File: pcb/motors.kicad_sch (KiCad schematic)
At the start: 21 parts, among them J4 Conn_01x02_Pin, J5 Conn_01x02_Pin, J6 Conn_01x02_Pin, J7 Conn_01x02_Pin, J8 Conn_01x02_Pin, Q1 AO3400A, U3 DRV8833PWP, U4 DRV8833PWP

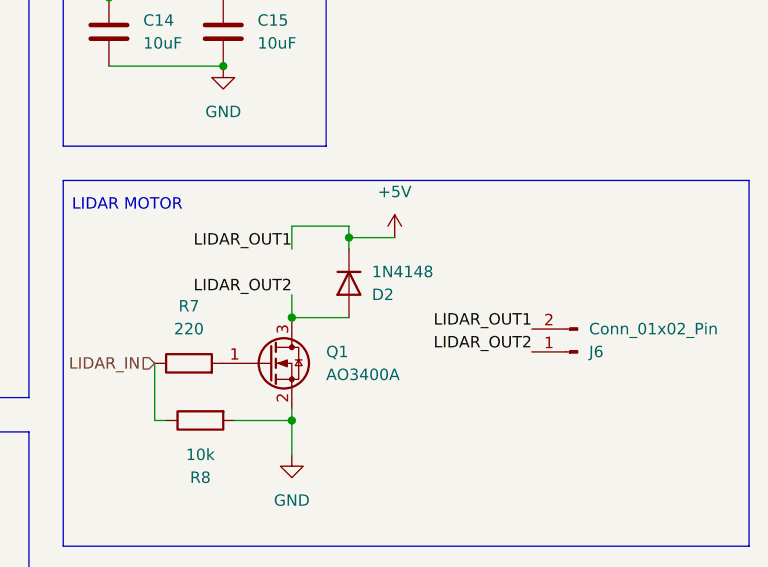
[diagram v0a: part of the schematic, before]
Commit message: update diode, usb routing
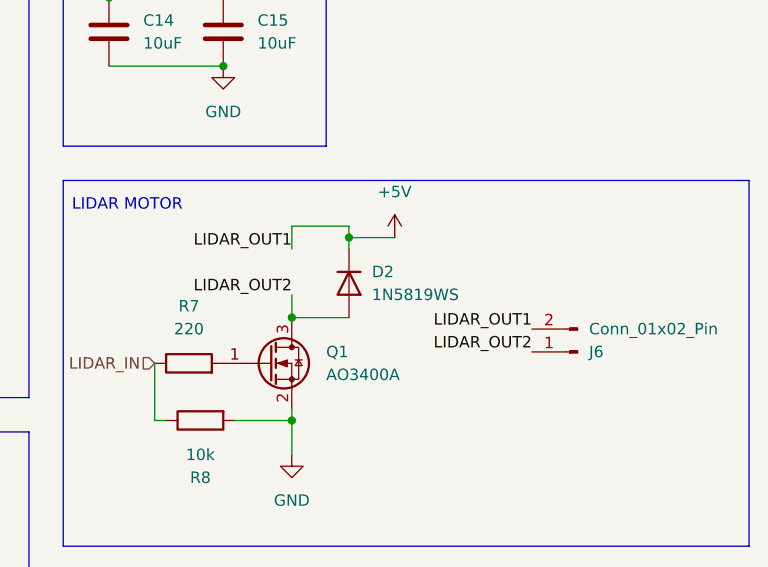
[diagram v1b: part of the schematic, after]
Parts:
- D2: value 1N4148 -> 1N5819WS; footprint Diode_SMD:D_SOD-323_HandSoldering -> Diode_SMD:D_SOD-123; LCSC C41371421 -> C8598
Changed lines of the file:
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@@
+	)
+	(symbol
+		(lib_id "Device:D")
+		(at 142.24 63.5 270)
+		(unit 1)
+		(body_style 1)
+		(exclude_from_sim no)
+		(in_bom no)
+		(on_board yes)
+		(in_pos_files yes)
+		(dnp no)
+		(fields_autoplaced yes)
+		(property "Reference" "D2"
+			(at 144.78 62.2299 90)
+			(show_name no)
+			(do_not_autoplace no)
+			(effects
+				(font
+					(size 1.27 1.27)
+				)
+				(justify left)
+			)
+		)
+		(property "Value" "1N5819WS"
+			(at 144.78 64.7699 90)
+			(show_name no)
+			(do_not_autoplace no)
+			(effects
+				(font
+					(size 1.27 1.27)
+				)
+				(justify left)
+			)
+		)
+		(property "Footprint" "Diode_SMD:D_SOD-123"
+			(at 142.24 63.5 0)
+			(hide yes)
+			(show_name no)
+			(do_not_autoplace no)
+			(effects
+				(font
+					(size 1.27 1.27)
+				)
+			)
+		)
+		(property "Datasheet" ""
+			(at 142.24 63.5 0)
+			(hide yes)
+			(show_name no)
+			(do_not_autoplace no)
+			(effects
+				(font
+					(size 1.27 1.27)
+				)
+			)
+		)
+		(property "Description" "Diode"
+			(at 142.24 63.5 0)
+			(hide yes)
+			(show_name no)
+			(do_not_autoplace no)
+			(effects
+				(font
+					(size 1.27 1.27)
+				)
+			)
+		)
+		(property "Sim.Device" "D"
+			(at 142.24 63.5 0)
+			(hide yes)
+			(show_name no)
+			(do_not_autoplace no)
+			(effects
+				(font
+					(size 1.27 1.27)
+				)
+			)
+		)
+		(property "Sim.Pins" "1=K 2=A"
+			(at 142.24 63.5 0)
+			(hide yes)
+			(show_name no)
+			(do_not_autoplace no)
+			(effects
+				(font
+					(size 1.27 1.27)
+				)
+			)
+		)
+		(property "LCSC" "C8598"
+			(at 142.24 63.5 0)
+			(hide yes)
+			(show_name no)
+			(do_not_autoplace no)
+			(effects
+				(font
+					(size 1.27 1.27)
+				)
+			)
+		)
+		(property "KLC_S3.3" ""
+			(at 142.24 63.5 0)
+			(hide yes)
+			(show_name no)
+			(do_not_autoplace no)
+			(effects
+				(font
+					(size 1.27 1.27)
+				)
+			)
+		)
+		(property "KLC_S4.1" ""
+			(at 142.24 63.5 0)
+			(hide yes)
+			(show_name no)
+			(do_not_autoplace no)
+			(effects
+				(font
+					(size 1.27 1.27)
+				)
+			)
+		)
+		(pin "2"
+		)
+		(pin "1"
+		)
+		(instances
+			(project "slam"
+				(path "/d9b72bf7-a9fc-47a9-9340-f48fc87a9331/33a751a0-247f-4347-86aa-bb0fbce908f1"
+					(reference "D2")
+					(unit 1)
+				)
+			)
+		)
 	)
 	(symbol
@@
 					(unit 1)
 				)
-			)
-		)
-	)
-	(symbol
-		(lib_id "Device:D")
-		(at 142.24 63.5 90)
-		(mirror x)
-		(unit 1)
-		(body_style 1)
-		(exclude_from_sim no)
-		(in_bom no)
-		(on_board yes)
-		(in_pos_files yes)
-		(dnp no)
-		(property "Reference" "D2"
-			(at 144.78 64.7701 90)
-			(show_name no)
-			(do_not_autoplace no)
-			(effects
-				(font
-					(size 1.27 1.27)
-				)
-				(justify right)
-			)
-		)
-		(property "Value" "1N4148"
-			(at 144.78 62.2301 90)
-			(show_name no)
-			(do_not_autoplace no)
-			(effects
-				(font
-					(size 1.27 1.27)
-				)
-				(justify right)
-			)
-		)
-		(property "Footprint" "Diode_SMD:D_SOD-323_HandSoldering"
-			(at 142.24 63.5 0)
-			(hide yes)
-			(show_name no)
-			(do_not_autoplace no)
-			(effects
-				(font
-					(size 1.27 1.27)
-				)
-			)
-		)
-		(property "Datasheet" ""
-			(at 142.24 63.5 0)
-			(hide yes)
-			(show_name no)
-			(do_not_autoplace no)
-			(effects
-				(font
-					(size 1.27 1.27)
-				)
-			)
-		)
-		(property "Description" "Diode"
-			(at 142.24 63.5 0)
-			(hide yes)
-			(show_name no)
-			(do_not_autoplace no)
-			(effects
-				(font
-					(size 1.27 1.27)
-				)
-			)
-		)
-		(property "Sim.Device" "D"
-			(at 142.24 63.5 0)
-			(hide yes)
-			(show_name no)
-			(do_not_autoplace no)
-			(effects
-				(font
-					(size 1.27 1.27)
-				)
-			)
-		)
-		(property "Sim.Pins" "1=K 2=A"
-			(at 142.24 63.5 0)
-			(hide yes)
-			(show_name no)
-			(do_not_autoplace no)
-			(effects
-				(font
-					(size 1.27 1.27)
-				)
-			)
-		)
-		(property "LCSC" "C41371421"
-			(at 142.24 63.5 90)
-			(hide yes)
-			(show_name no)
-			(do_not_autoplace no)
-			(effects
-				(font
-					(size 1.27 1.27)
-				)
-			)
-		)
-		(property "KLC_S3.3" ""
-			(at 142.24 63.5 90)
-			(hide yes)
-			(show_name no)
-			(do_not_autoplace no)
-			(effects
-				(font
-					(size 1.27 1.27)
-				)
-			)
-		)
-		(property "KLC_S4.1" ""
-			(at 142.24 63.5 90)
-			(hide yes)
-			(show_name no)
-			(do_not_autoplace no)
-			(effects
-				(font
-					(size 1.27 1.27)
-				)
-			)
-		)
-		(pin "1"
-		)
-		(pin "2"
-		)
-		(instances
-			(project "slam"
-				(path "/d9b72bf7-a9fc-47a9-9340-f48fc87a9331/33a751a0-247f-4347-86aa-bb0fbce908f1"
-					(reference "D2")
-					(unit 1)
-				)
